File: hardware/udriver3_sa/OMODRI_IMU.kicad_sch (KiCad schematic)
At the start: 5 parts, among them U7 BMI088

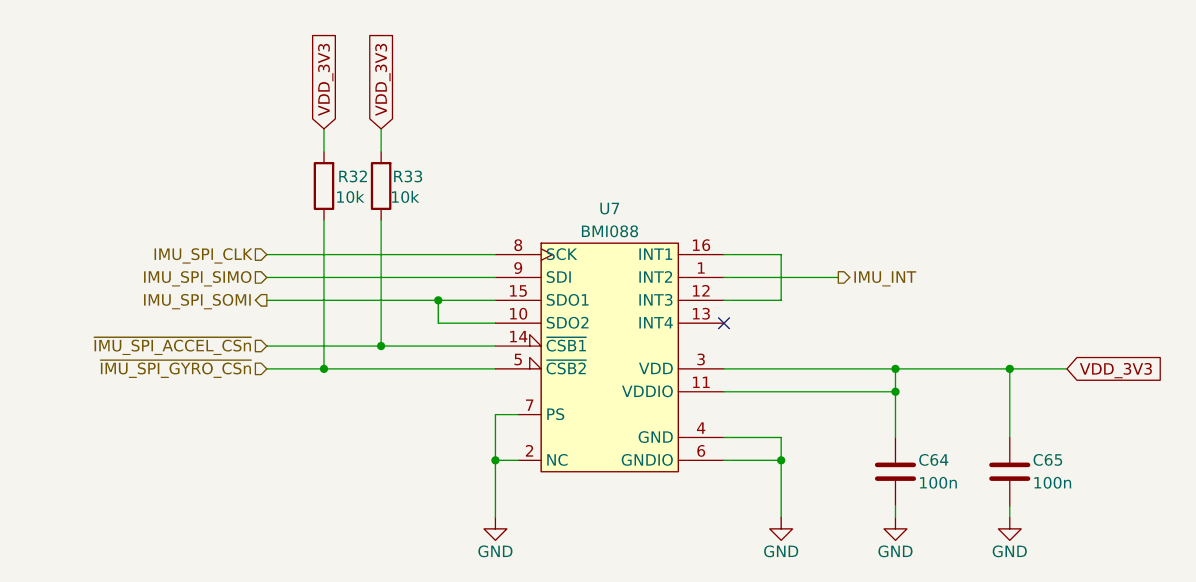
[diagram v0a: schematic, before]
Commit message: Update on uOmodri_SA. Remove USB, com SPI & debug connectors for integration into Myactuator motors. Connectors replaced by a ZIF connector.
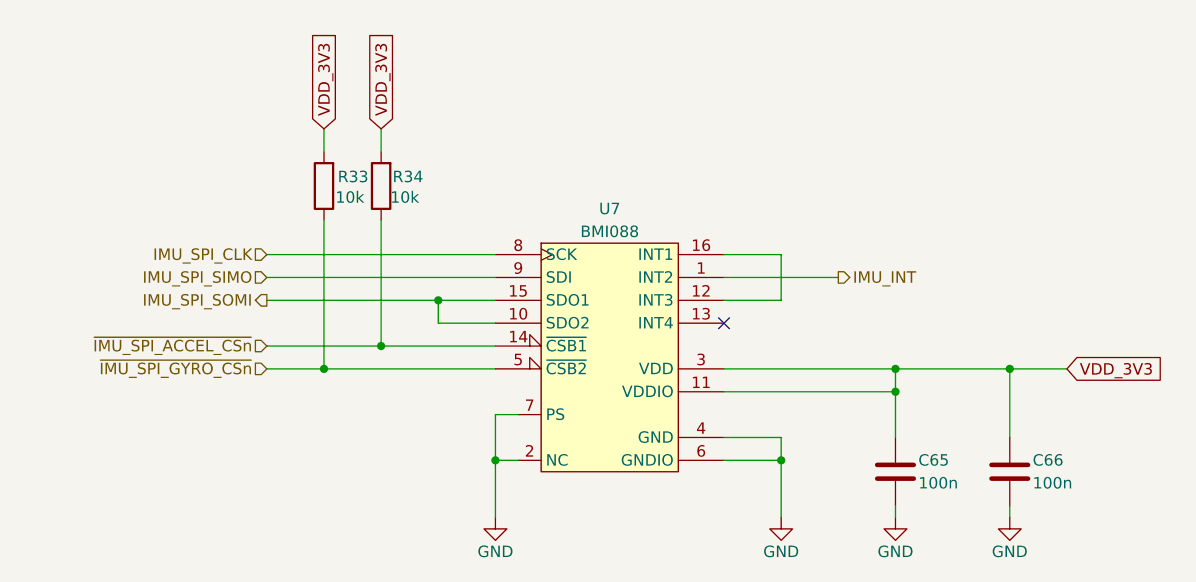
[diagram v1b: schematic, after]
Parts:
- renumbered C64 to C65, C65 to C66, R32 to R33, R33 to R34
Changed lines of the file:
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@@
 	(title_block
 		(title "Open MOtor DRiver Initiative  - Single Axis (OMODRI_SA)")
-		(date "2024-03-20")
+		(date "2024-11-08")
 		(rev "1.0")
 		(company "LAAS/CNRS")
@@
 		(on_board yes)
 		(dnp no)
-		(property "Reference" "C64"
+		(property "Reference" "C65"
 			(at 193.04 100.33 0)
 			(effects
@@
 			(project "omodri_sa_laas"
 				(path "/de5b13f0-933a-4c4d-9979-13dc57b13241/4fa0662b-a85d-4e25-9d18-e8dd09c83e01"
-					(reference "C64")
+					(reference "C65")
 					(unit 1)
 				)
@@
 		(on_board yes)
 		(dnp no)
-		(property "Reference" "R33"
+		(property "Reference" "R34"
 			(at 134.62 68.834 0)
 			(effects
@@
 			(project "omodri_sa_laas"
 				(path "/de5b13f0-933a-4c4d-9979-13dc57b13241/4fa0662b-a85d-4e25-9d18-e8dd09c83e01"
-					(reference "R33")
+					(reference "R34")
 					(unit 1)
 				)
@@
 		(on_board yes)
 		(dnp no)
-		(property "Reference" "#PWR0100"
+		(property "Reference" "#PWR091"
 			(at 190.5 113.03 0)
 			(effects
@@
 			(project "omodri_sa_laas"
 				(path "/de5b13f0-933a-4c4d-9979-13dc57b13241/4fa0662b-a85d-4e25-9d18-e8dd09c83e01"
-					(reference "#PWR0100")
+					(reference "#PWR091")
 					(unit 1)
 				)
@@
 		(on_board yes)
 		(dnp no)
-		(property "Reference" "#PWR099"
+		(property "Reference" "#PWR090"
 			(at 177.8 113.03 0)
 			(effects
@@
 			(project "omodri_sa_laas"
 				(path "/de5b13f0-933a-4c4d-9979-13dc57b13241/4fa0662b-a85d-4e25-9d18-e8dd09c83e01"
-					(reference "#PWR099")
+					(reference "#PWR090")
 					(unit 1)
 				)
@@
 		(on_board yes)
 		(dnp no)
-		(property "Reference" "C65"
+		(property "Reference" "C66"
 			(at 205.74 100.33 0)
 			(effects
@@
 			(project "omodri_sa_laas"
 				(path "/de5b13f0-933a-4c4d-9979-13dc57b13241/4fa0662b-a85d-4e25-9d18-e8dd09c83e01"
-					(reference "C65")
+					(reference "C66")
 					(unit 1)
 				)
@@
 		(on_board yes)
 		(dnp no)
-		(property "Reference" "#PWR098"
+		(property "Reference" "#PWR089"
 			(at 146.05 113.03 0)
 			(effects
@@
 			(project "omodri_sa_laas"
 				(path "/de5b13f0-933a-4c4d-9979-13dc57b13241/4fa0662b-a85d-4e25-9d18-e8dd09c83e01"
-					(reference "#PWR098")
+					(reference "#PWR089")
 					(unit 1)
 				)
@@
 		(on_board yes)
 		(dnp no)
-		(property "Reference" "R32"
+		(property "Reference" "R33"
 			(at 128.524 68.834 0)
 			(effects
@@
 			(project "omodri_sa_laas"
 				(path "/de5b13f0-933a-4c4d-9979-13dc57b13241/4fa0662b-a85d-4e25-9d18-e8dd09c83e01"
-					(reference "R32")
+					(reference "R33")
 					(unit 1)
 				)
@@
 		(on_board yes)
 		(dnp no)
-		(property "Reference" "#PWR0101"
+		(property "Reference" "#PWR092"
 			(at 203.2 113.03 0)
 			(effects
@@
 			(project "omodri_sa_laas"
 				(path "/de5b13f0-933a-4c4d-9979-13dc57b13241/4fa0662b-a85d-4e25-9d18-e8dd09c83e01"
-					(reference "#PWR0101")
+					(reference "#PWR092")
 					(unit 1)
 				)
